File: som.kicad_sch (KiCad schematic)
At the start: 34 parts, among them M1 Jetson-Orin-NX-Nano, U4 NTS0102_XSON

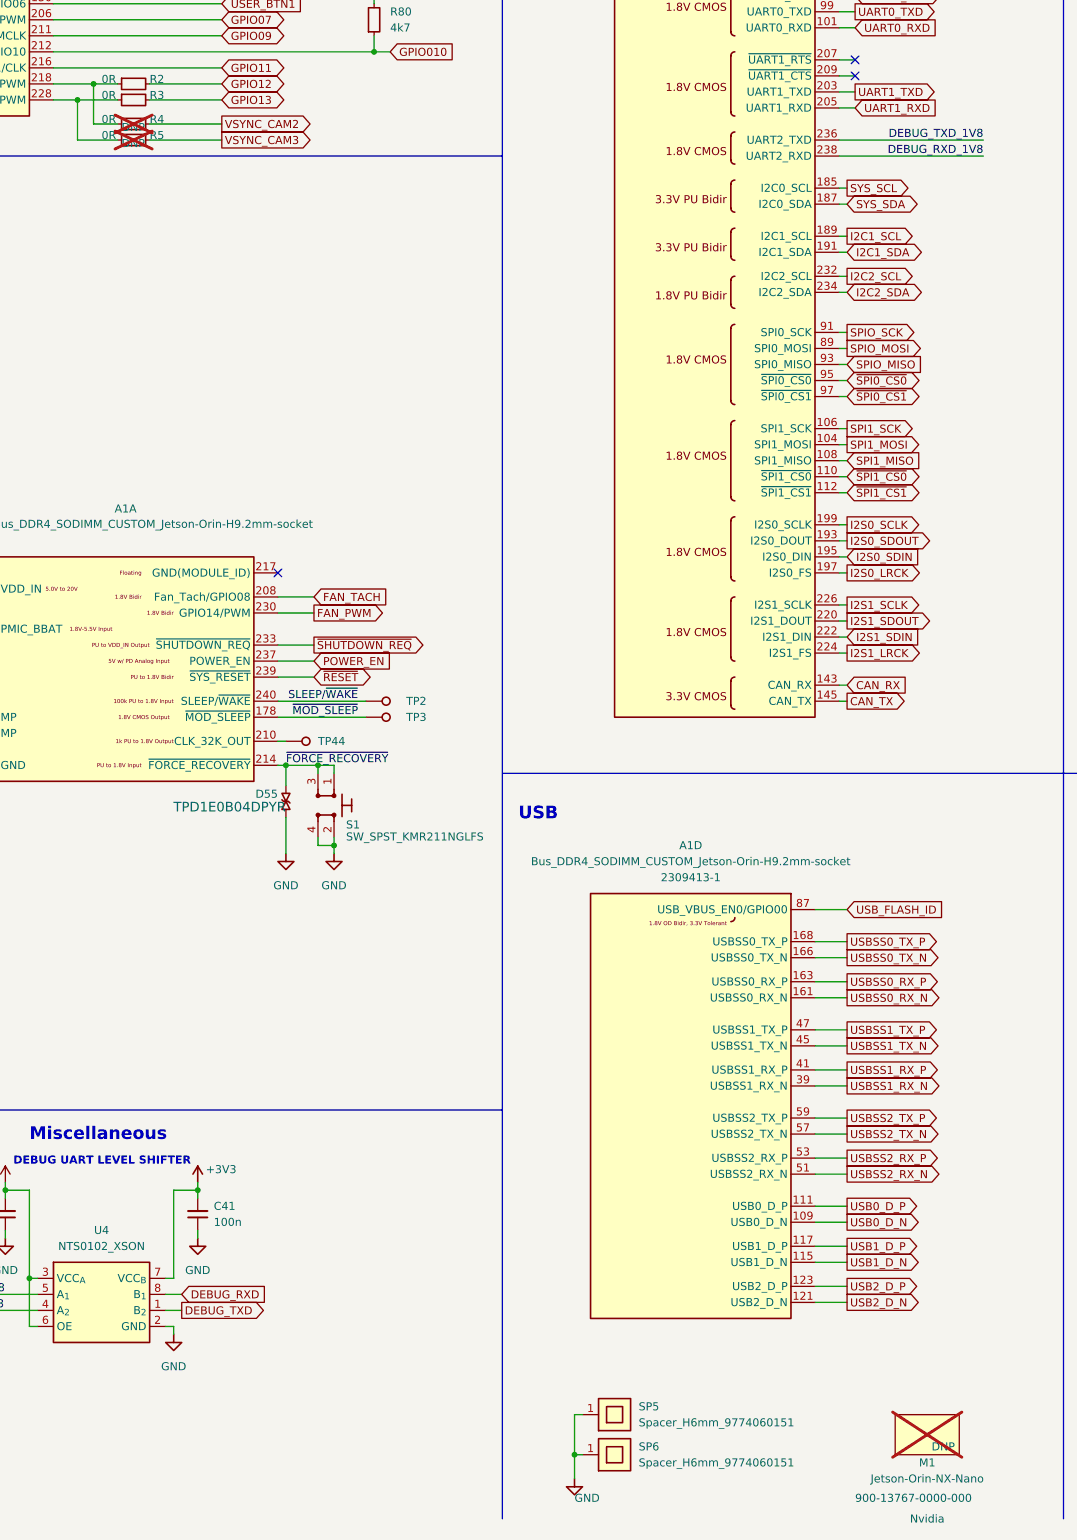
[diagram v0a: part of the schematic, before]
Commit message: 5/16 Commit: Sch Mods added and beginning Development on PCB layout
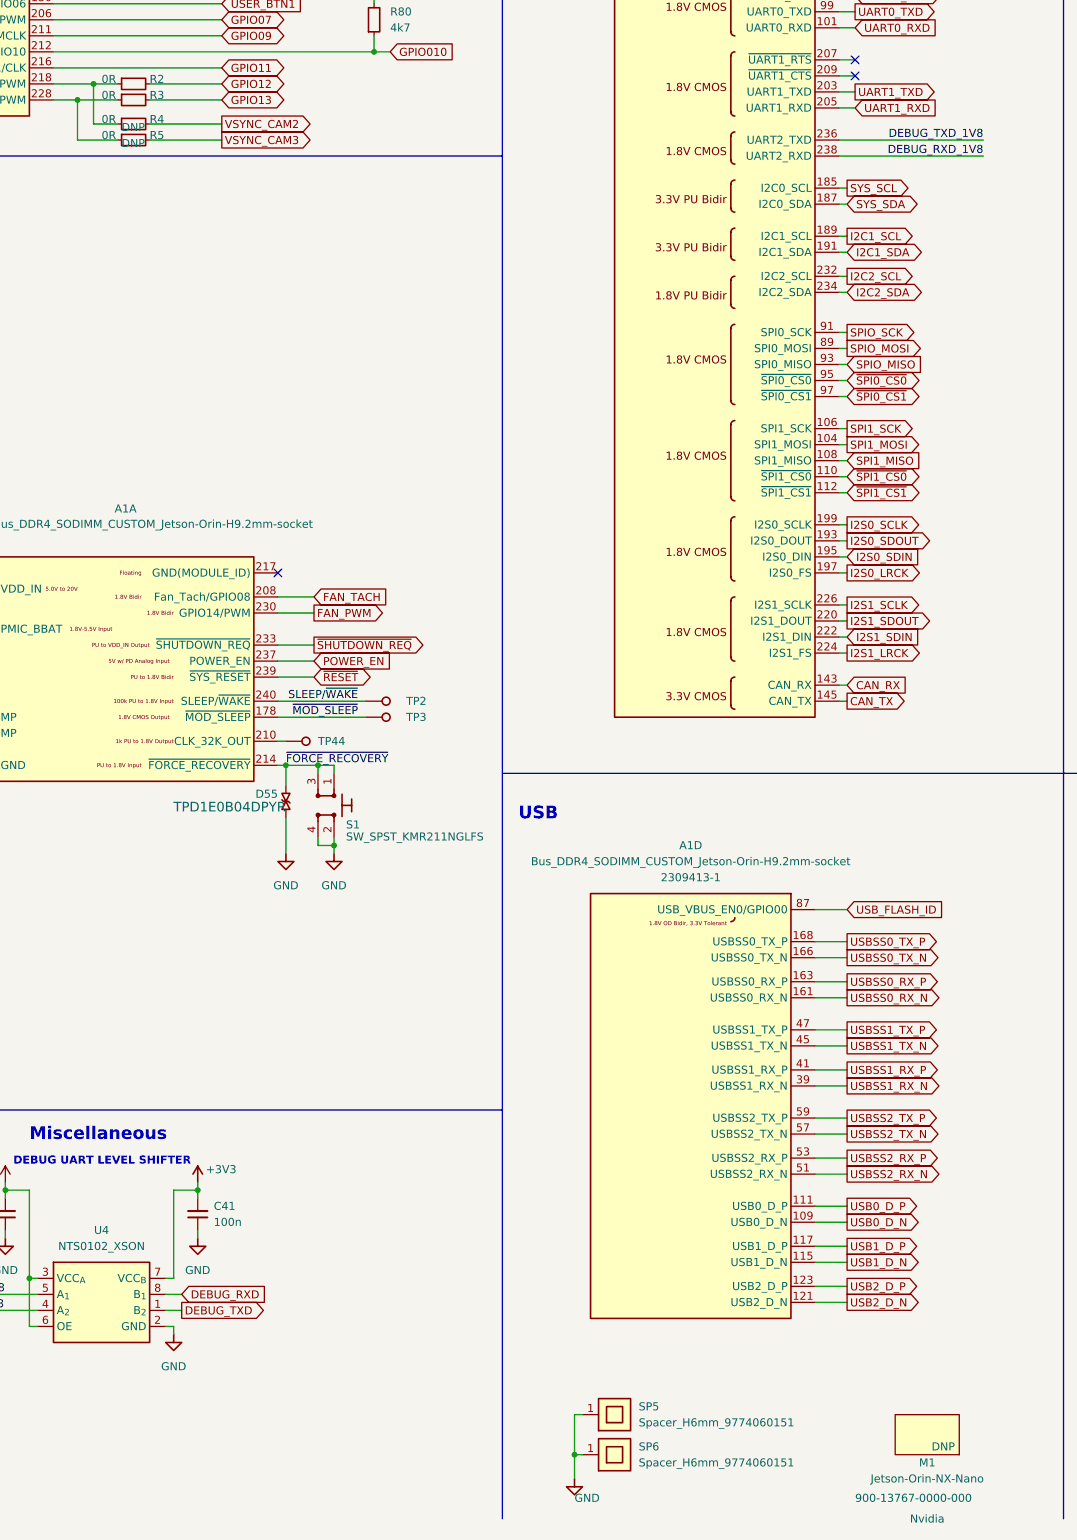
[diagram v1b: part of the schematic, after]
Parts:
- M1, R4, R5: now fitted
